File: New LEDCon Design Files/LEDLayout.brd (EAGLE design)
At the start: 81.7 x 51.7 mm, 7 parts

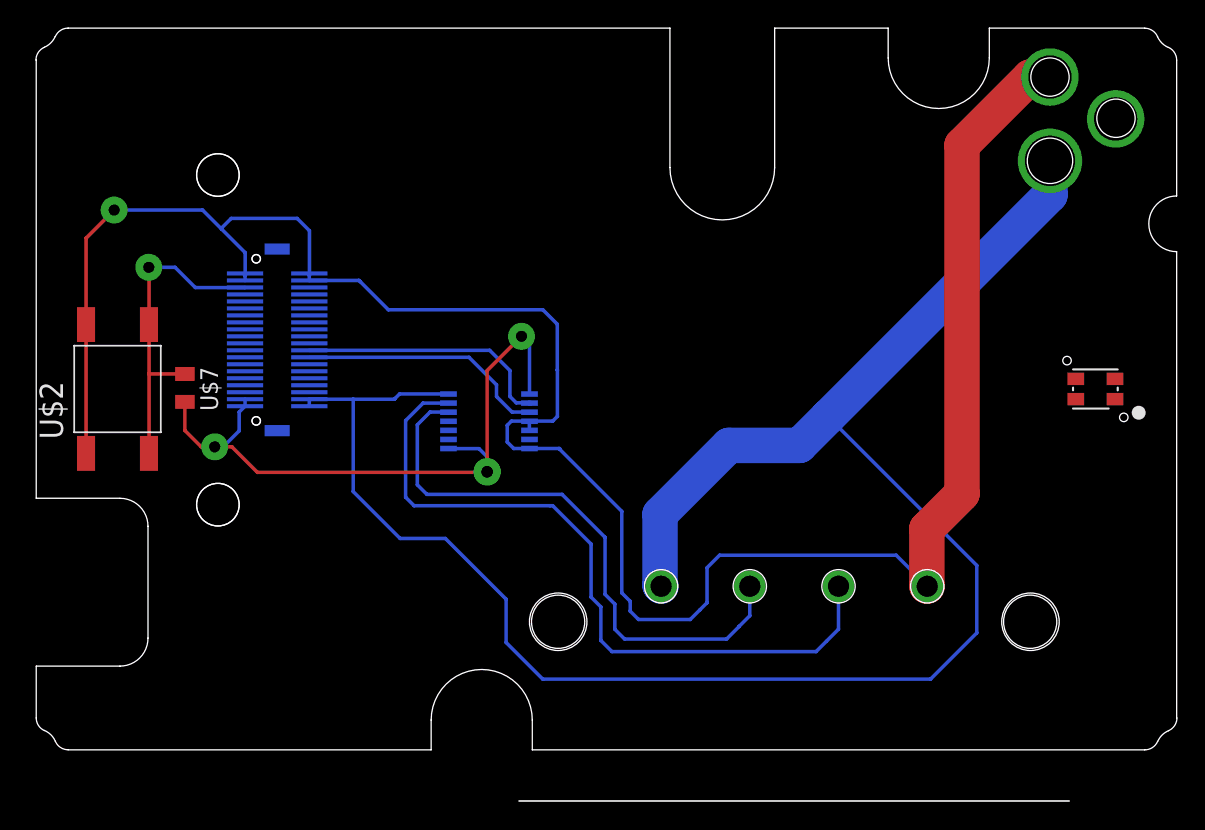
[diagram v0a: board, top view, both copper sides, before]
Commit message: Finished routing 1st prototype
Added WS2801, choice resistors & finished routing
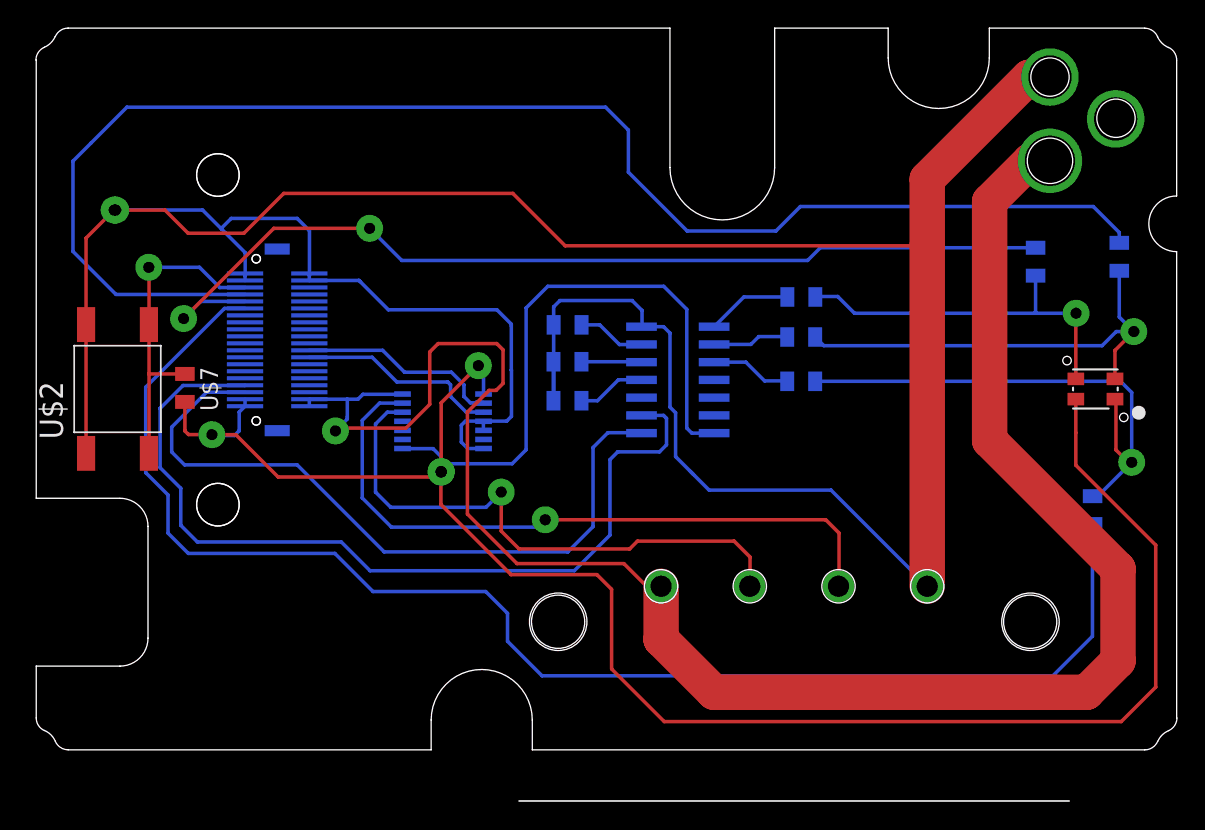
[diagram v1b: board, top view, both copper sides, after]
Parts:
- added U$10, U$11, U$12, U$13, U$14, U$15, U$16, U$17, U$9: (no value), GW-devices:RF-C0805
- added U$8: WS2801, GW-devices:SO14
- moved U$6 3.29 mm to (-11.7, -2.31)
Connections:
- new net N$10: U$4.P$33, U$8.2
- new net N$11: U$15.1, U$8.6
- new net N$12: U$16.1, U$8.5
- new net N$13: U$17.1, U$8.4
- new net N$14: U$4.P$35, U$8.1
- new net N$15: U$14.1, U$4.P$7
- new net N$16: U$13.1, U$4.P$9
- new net N$17: U$12.1, U$4.P$11
- new net N$7: U$11.1, U$12.2, U$5.P$1
- new net N$8: U$10.2, U$8.8
- new net N$9: U$8.9, U$9.2
- net +3V3: now also U$8.14
- net GND: now also U$15.2, U$16.2, U$17.2, U$8.7
- net N$4: now also U$14.2, U$9.1
- net N$5: now also U$10.1, U$13.2
- net N$6: now also U$11.2, U$8.10; no longer U$5.P$1
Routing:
- net +3V3: track 48.8 -> 169.3 mm
- net N$15: track 0.00 -> 104.2 mm
- net N$17: track 0.00 -> 101.4 mm
- net N$16: track 0.00 -> 70.5 mm, vias 0 -> 2
- net GND: track 157.6 -> 222.4 mm, vias 1 -> 2
- net N$10: track 0.00 -> 62.6 mm
- net N$14: track 0.00 -> 51.5 mm
- net N$7: track 0.00 -> 37.0 mm, vias 0 -> 1
- net N$4: track 0.00 -> 32.2 mm, vias 0 -> 1
- net N$5: track 0.00 -> 26.6 mm, vias 0 -> 1
- net N$8: track 0.00 -> 6.12 mm
- net N$6: track 0.00 -> 5.85 mm
- net N$9: track 0.00 -> 5.47 mm
- net N$13: track 0.00 -> 4.93 mm
- net N$11: track 0.00 -> 4.88 mm
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
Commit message: Added JTAG header, fixed data / clock switch
Moved TXB0104 to front side
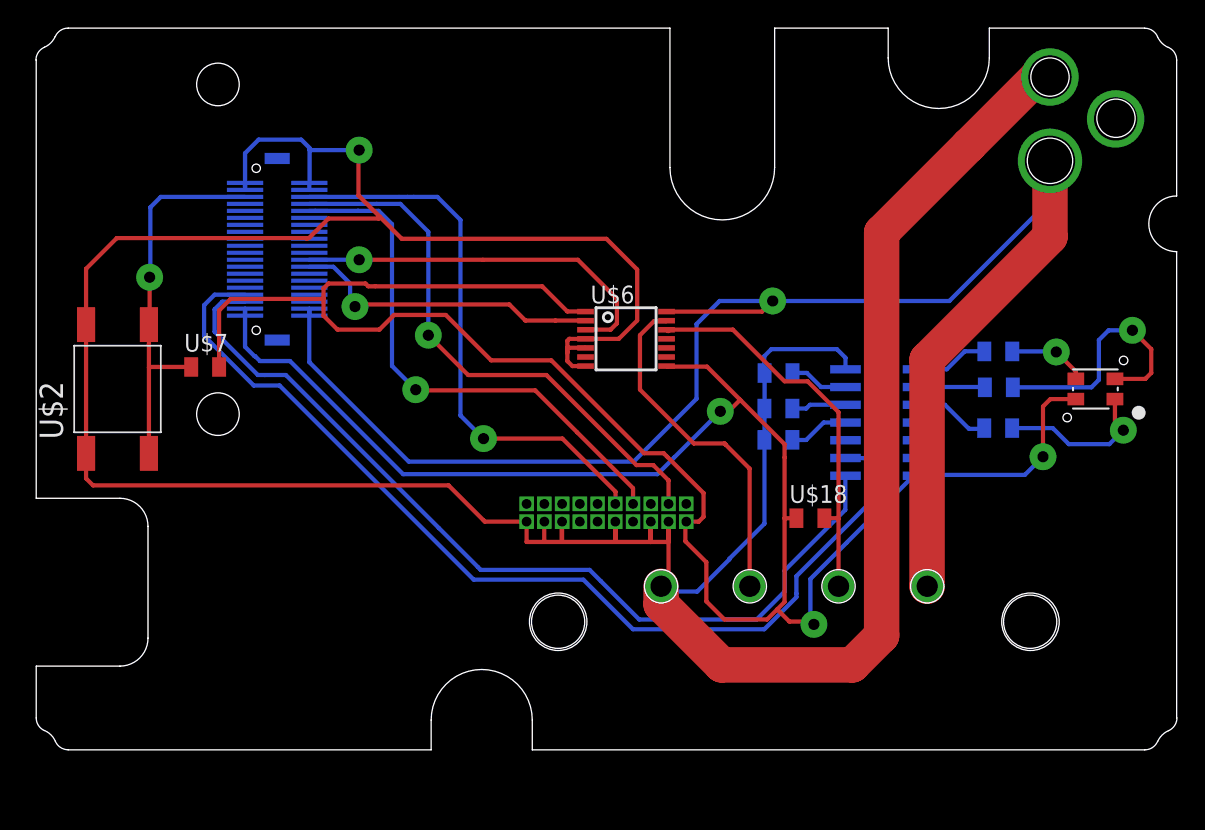
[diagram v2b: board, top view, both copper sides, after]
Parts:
- removed U$12, U$13, U$14: (no value), GW-devices:RF-C0805
- added U$18: (no value), GW-devices:RF-C0805
- added U$19: 2X10JTAG, KW2:2X10JTAG
- moved U$1 19.1 mm to (3.91, -14.1), flipped to the bottom
- moved U$15 15.5 mm to (12.3, 1.14)
- moved U$16 15.5 mm to (12.3, -1.40)
- moved U$17 15.4 mm to (12.3, -3.64)
- moved U$8 14.9 mm to (19.7, -2.40)
- moved U$10 14.6 mm to (28.1, 2.69)
- moved U$9 14.6 mm to (28.1, 0.12)
- moved U$11 14.5 mm to (28.0, -2.80)
- moved U$6 14.4 mm to (1.40, 3.59), flipped to the top
- moved U$4 6.48 mm to (-23.6, 10.0)
- moved U$7 2.08 mm to (-28.7, 1.57), turned to 0 degrees
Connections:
- removed net N$15: U$14.1, U$4.P$7
- removed net N$16: U$13.1, U$4.P$9
- removed net N$17: U$12.1, U$4.P$11
- new net N$18: U$19.P$4, U$4.P$8
- new net N$19: U$4.P$14
- new net N$20: U$19.P$8, U$4.P$10
- new net N$21: U$19.P$10, U$4.P$6
- new net N$22: U$4.P$12
- net +3V3: now also U$18.1, U$19.P$1
- net CLK_5V: now also U$1.P$3, U$18.2, U$6.12; no longer U$1.P$2, U$6.13
- net DAT_5V: now also U$1.P$2, U$6.13; no longer U$1.P$3, U$6.12
- net GND: now also U$19.P$15, U$19.P$17, U$19.P$19, U$19.P$3, U$19.P$5, U$19.P$9
- net N$1: now also U$4.P$26; no longer U$4.P$24
- net N$2: now also U$4.P$24; no longer U$4.P$26
- net N$4: no longer U$14.2
- net N$5: no longer U$13.2
- net N$7: no longer U$12.2
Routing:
- net N$15: track 104.2 -> 0.00 mm
- net N$17: track 101.4 -> 0.00 mm
- net N$16: track 70.5 -> 0.00 mm, vias 2 -> 0
- net N$18: track 0.00 -> 39.9 mm, vias 0 -> 1
- net N$21: track 0.00 -> 39.7 mm, vias 0 -> 1
- net N$20: track 0.00 -> 38.5 mm, vias 0 -> 1
- net N$7: track 37.0 -> 11.3 mm
- net GND: track 222.4 -> 247.0 mm, vias 2 -> 1
- net V+: track 137.2 -> 116.0 mm
- net N$5: track 26.6 -> 5.67 mm
- net CLK_5V: track 48.4 -> 28.3 mm, vias 1 -> 0
- net DAT_5V: track 41.0 -> 25.0 mm, vias 1 -> 0
- net +3V3: track 169.3 -> 183.5 mm, vias 4 -> 3
- net N$4: track 32.2 -> 18.3 mm
- net N$2: track 14.6 -> 27.4 mm, vias 0 -> 1
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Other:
- outline, holes or cut-outs redrawn

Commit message: Prototype 3
Added filter caps and output data /clk pullups
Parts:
- added U$12, U$13: (no value), GW-devices:C0402
- added U$14: (no value), GW-devices:RF-R0402
- added U$20, U$21: (no value), GW-devices:RF-C0805
- added U$22, U$23: (no value), GW-devices:C0805
- U$18: device GW-devices:RF-C0805 -> GW-devices:RF-R0402
- moved U$18 10.6 mm to (9.00, -0.30), turned to 270 degrees
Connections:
- net +3V3: now also U$13.1, U$22.1; no longer U$18.1, U$4.P$39
- net CLK_5V: now also U$20.2
- net DAT_5V: now also U$14.1, U$21.1
- net GND: now also U$12.2, U$13.2, U$22.2, U$23.2
- net V+: now also U$12.1, U$14.2, U$18.1, U$20.1, U$21.2, U$23.1
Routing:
- net +3V3: track 183.5 -> 150.1 mm
- net V+: track 116.0 -> 135.1 mm
- net GND: track 247.0 -> 261.1 mm
- net DAT_5V: track 25.0 -> 31.7 mm
- net N$20: track 38.5 -> 42.5 mm
- net N$18: track 39.9 -> 42.8 mm
- net CLK_5V: track 28.3 -> 26.9 mm
- net N$1: track 22.3 -> 21.4 mm
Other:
- outline, holes or cut-outs redrawn
- board text added: "LEDCON.PCB.v1.0.P3"

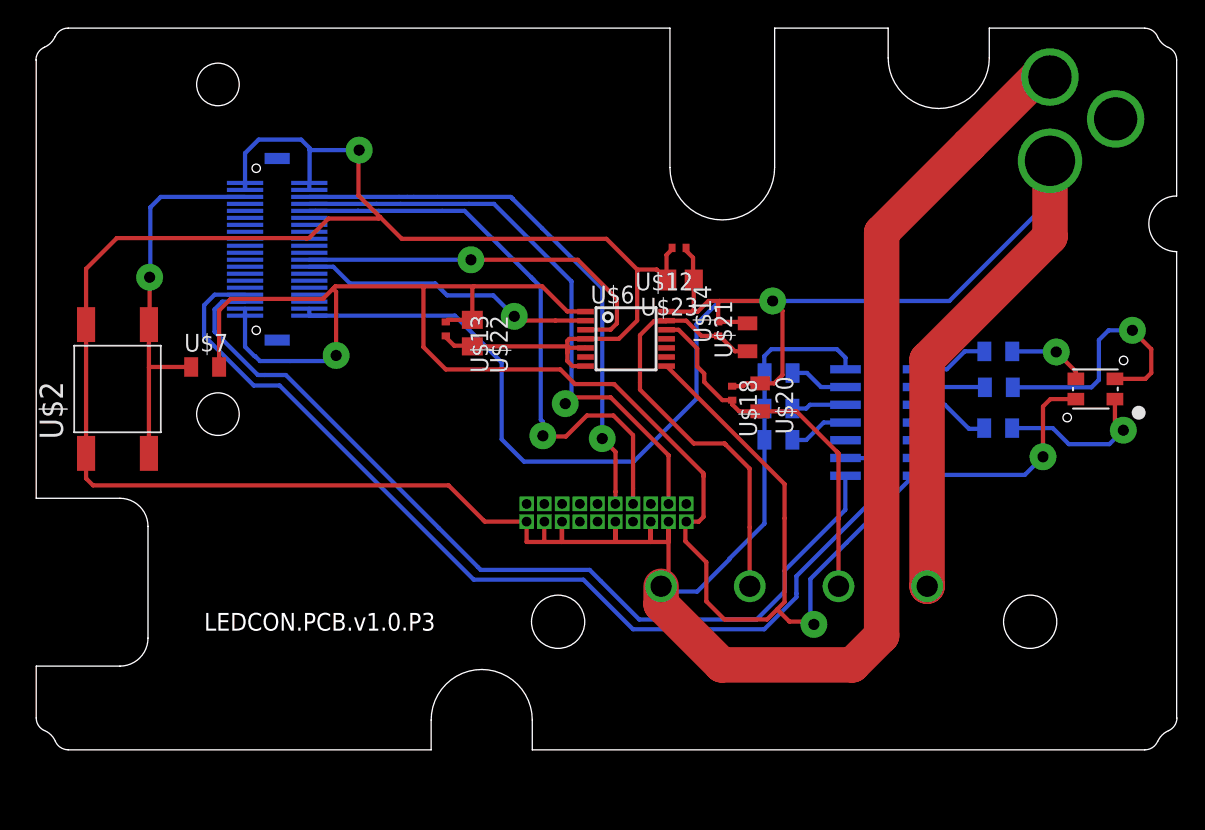
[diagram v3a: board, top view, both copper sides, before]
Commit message: Prototype 4
Fixed LED, removed jumpers, fixed JTAG traces and added RA reset button
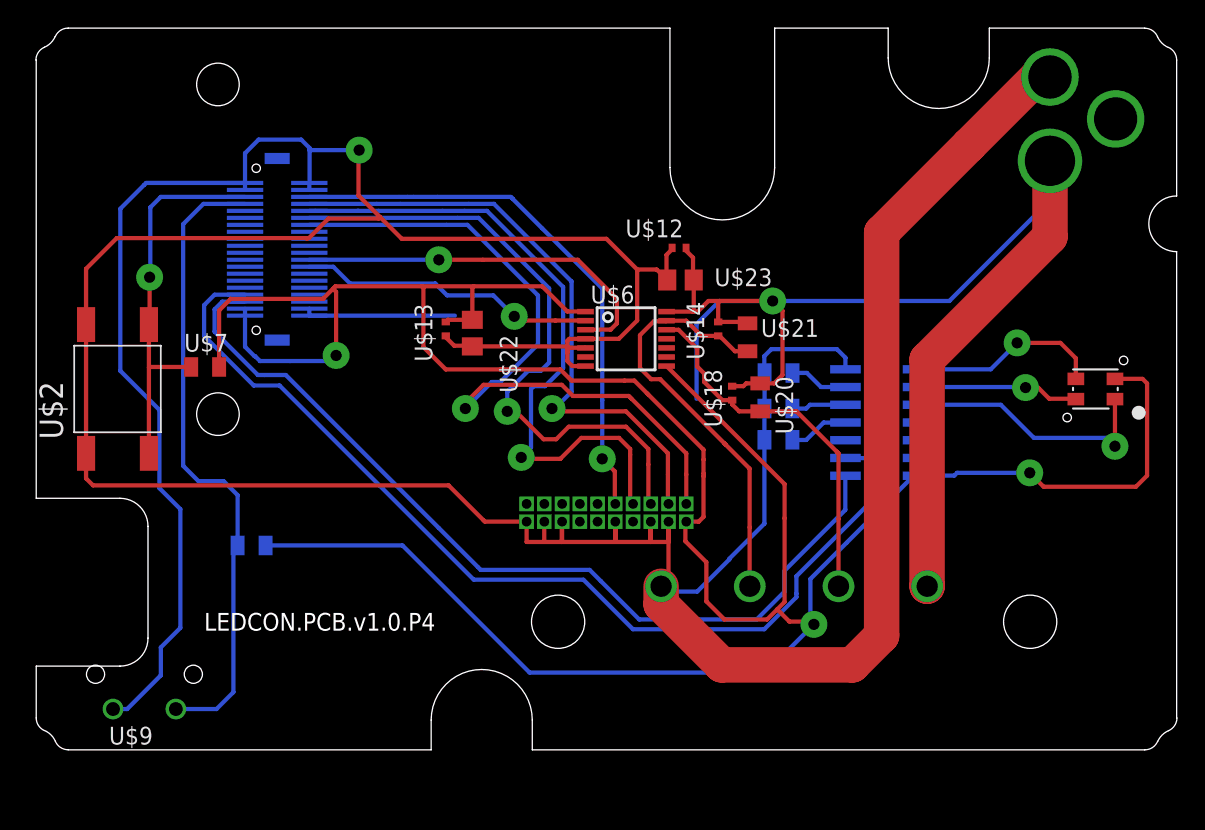
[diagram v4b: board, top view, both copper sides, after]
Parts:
- removed U$11: (no value), GW-devices:RF-C0805
- U$9: value (none) -> RA_BUTTON; device GW-devices:RF-C0805 -> KW2:RA_BUTTON
- moved U$9 65.4 mm to (-33.1, -22.9), flipped to the top
- moved U$10 55.2 mm to (-25.4, -11.2), turned to 180 degrees
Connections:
- removed net N$19: U$4.P$14
- removed net N$22: U$4.P$12
- net +3V3: now also U$10.2, U$4.P$39
- net GND: now also U$9.P$1
- net N$4: now also U$8.9; no longer U$9.1
- net N$5: now also U$8.8; no longer U$10.1
- net N$6: now also U$19.P$2, U$4.P$14; no longer U$11.2, U$8.10
- net N$7: now also U$8.10; no longer U$11.1
- net N$8: now also U$19.P$6, U$4.P$12; no longer U$10.2, U$8.8
- net N$9: now also U$10.1, U$4.P$7, U$9.P$2; no longer U$8.9, U$9.2
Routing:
- net +3V3: track 150.1 -> 205.9 mm
- net GND: track 261.1 -> 310.4 mm
- net N$6: track 5.46 -> 51.5 mm, vias 0 -> 1
- net N$9: track 4.79 -> 45.9 mm
- net N$8: track 5.28 -> 45.8 mm, vias 0 -> 1
- net V+: track 135.1 -> 108.4 mm
- net N$5: track 5.67 -> 14.0 mm
- net N$7: track 11.3 -> 18.7 mm
- net N$4: track 18.3 -> 11.6 mm
- net N$20: track 42.5 -> 47.2 mm
- net N$18: track 42.8 -> 44.2 mm
- net DAT_5V: track 31.7 -> 30.8 mm
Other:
- board text added: "LEDCON.PCB.v1.0.P4"
- board text removed: "LEDCON.PCB.v1.0.P3"

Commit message: Prototype 5
Added Vreg, caps, fixed LED, assigned values & PNs, removed 0402
footprints. Pending exporting of production files
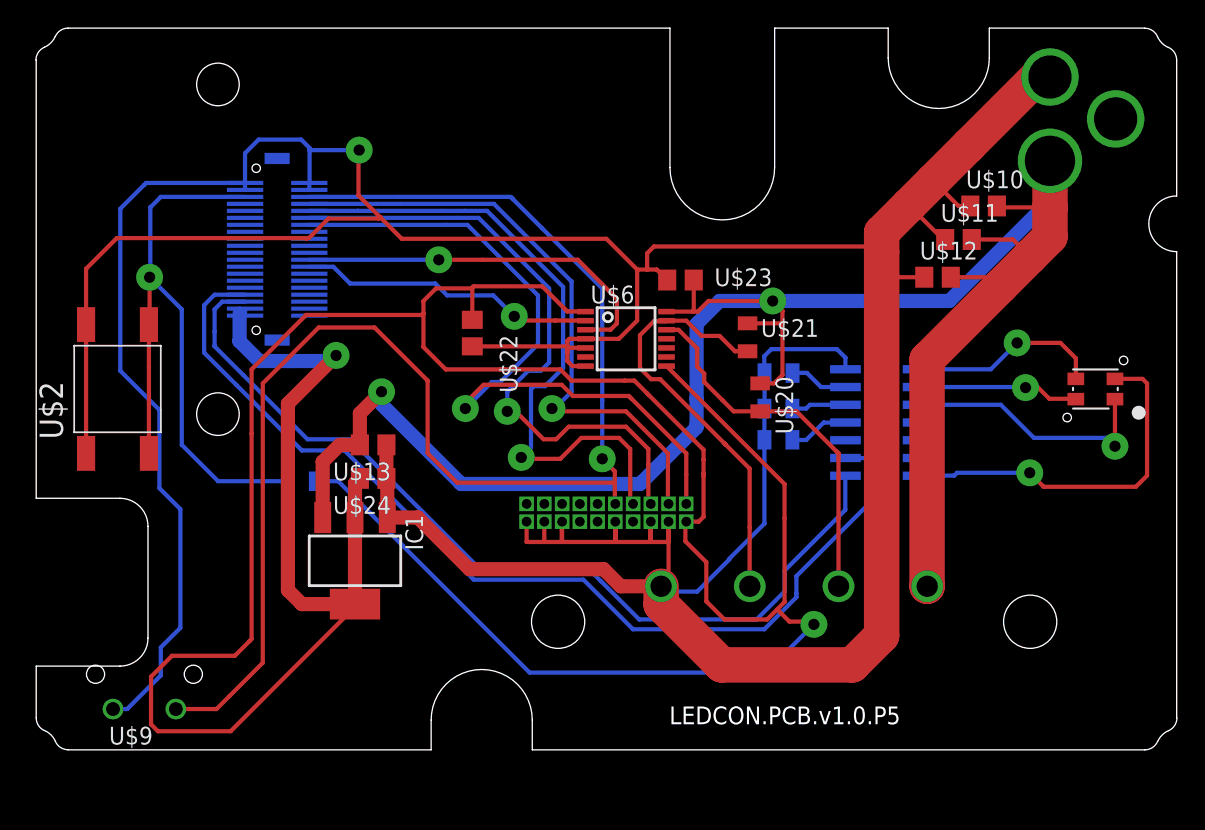
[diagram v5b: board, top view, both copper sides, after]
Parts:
- removed U$14, U$18: (no value), GW-devices:RF-R0402
- added IC1: (no value), KW2:SOT223
- added U$11: 1uF, GW-devices:C0805
- added U$24: 10uF, GW-devices:C0805
- U$1: value MATE-N-LOK_643230-1 -> (none)
- U$10: value (none) -> 0.1uF; device GW-devices:RF-C0805 -> GW-devices:C0805
- U$12, U$13: value (none) -> 10uF; device GW-devices:C0402 -> GW-devices:C0805
- U$15, U$16, U$17: value (none) -> 24Ohm
- U$19: value 2X10JTAG -> (none)
- U$2: value SWITCH-TACTILE -> (none)
- U$20, U$21: value (none) -> 68k
- U$22, U$23: value (none) -> 0.1uF
- U$3: value BARREL_CUI_PJ-002A -> (none)
- U$4: value DF12_F -> (none)
- U$5: value RGLBED -> (none)
- U$6: value TXB0104 -> (none)
- U$7: value (none) -> 10k
- U$8: value WS2801 -> (none)
- U$9: value RA_BUTTON -> (none)
- moved U$10 57.8 mm to (27.0, 13.1), flipped to the top, turned to 0 degrees
- moved U$12 18.6 mm to (23.7, 8.00), turned to 0 degrees
- moved U$7 10.7 mm to (-21.8, -6.60), flipped to the bottom, turned to 180 degrees
- moved U$13 9.79 mm to (-16.7, -4.00), turned to 180 degrees
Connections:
- removed net N$21 (its old number): U$19.P$10, U$4.P$6
- removed net N$9: U$10.1, U$4.P$7, U$9.P$2
- new net N$3: U$19.P$10, U$4.P$6, U$9.P$2
- net +3V3: now also IC1.2, IC1.4, U$24.2; no longer U$10.2, U$13.1, U$5.P$2, U$8.14
- net CLK_5V: no longer U$18.2
- net DAT_5V: no longer U$14.1
- net GND: now also IC1.1, U$10.1, U$11.1, U$12.1, U$13.1, U$24.1; no longer U$12.2, U$13.2
- net V+: now also IC1.3, U$10.2, U$11.2, U$12.2, U$13.2, U$5.P$2, U$8.14; no longer U$12.1, U$14.2, U$18.1, U$4.P$38, U$4.P$40
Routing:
- net N$3: track 0.00 -> 101.7 mm, vias 0 -> 1
- net V+: track 108.4 -> 179.3 mm, vias 1 -> 3
- net N$9: track 45.9 -> 0.00 mm
- net N$21 (its old number): track 39.6 -> 0.00 mm, vias 1 -> 0
- net +3V3: track 205.9 -> 234.5 mm, vias 3 -> 2
- net N$21: track 28.1 -> 46.7 mm
- net GND: track 310.4 -> 326.4 mm
- net N$10: track 71.6 -> 72.3 mm
- net N$14: track 64.3 -> 64.9 mm
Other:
- board text added: "LEDCON.PCB.v1.0.P5"
- board text removed: "LEDCON.PCB.v1.0.P4"
